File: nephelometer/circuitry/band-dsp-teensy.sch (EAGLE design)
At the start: 33 parts, among them IC1 LM4041CILP, IC2 AD822N, IC3 MCP6S21, J1 RJ11-6PTH, Q1 IRLB8721, T1 2N2222, T2 2N2222

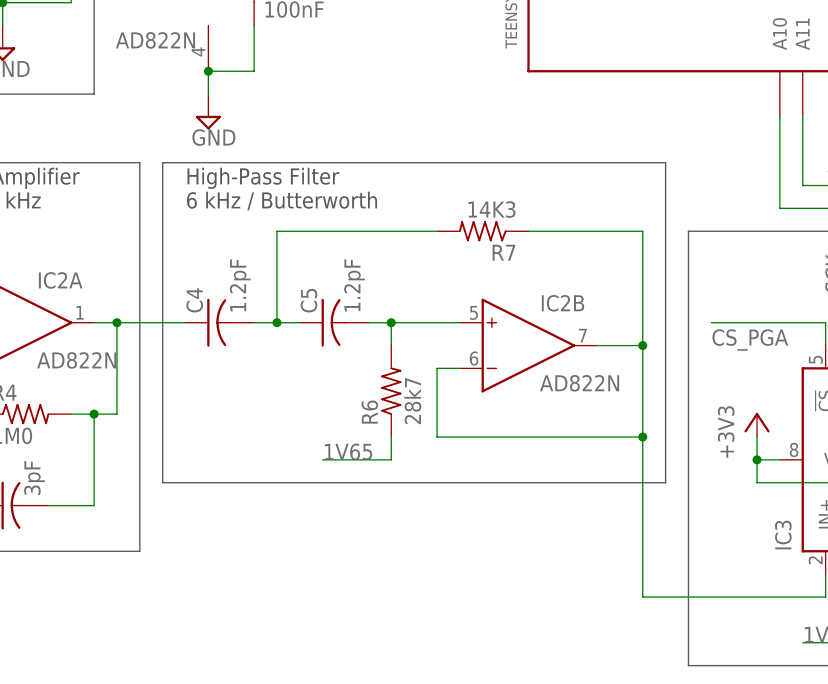
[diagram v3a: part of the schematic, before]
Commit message: Designed motor power board to stack on nephelometer or run over RJ11 cable
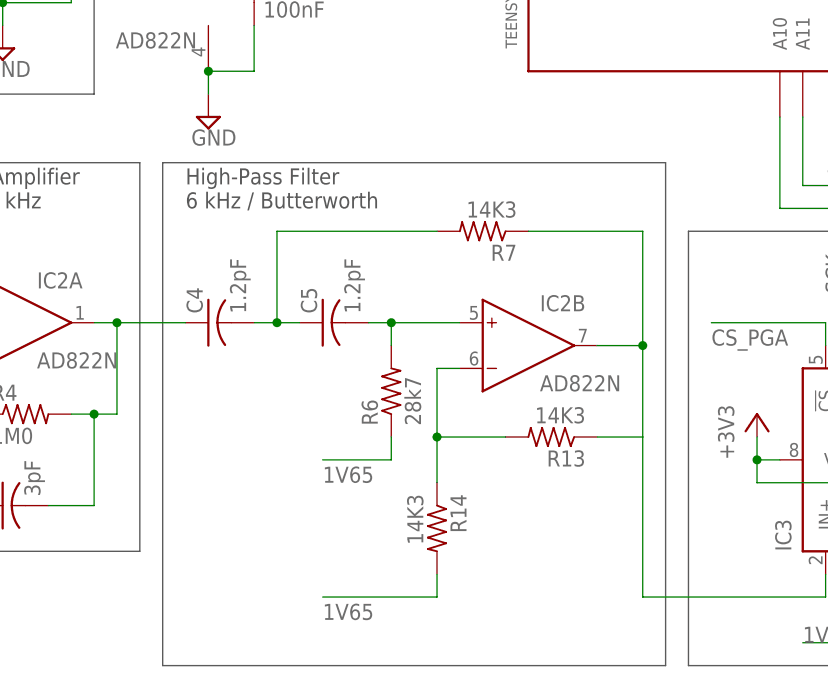
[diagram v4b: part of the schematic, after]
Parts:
- added R13, R14: 14K3, adafruit:R-US_0207/9
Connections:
- new net N$6: IC2B.IN-, R13.2, R14.1
- net 1V65: now also R14.2
- net N$3: now also R13.1; no longer IC2B.IN-
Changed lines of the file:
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@@
 <attribute name="MANF#" value="WP937AD/EGW"/>
+</part>
+<part name="R13" library="adafruit" deviceset="R-US_" device="0207/9" value="14K3">
+<attribute name="DIGIKEY#" value="14.3KXBK-ND"/>
+<attribute name="MANF" value="Yageo"/>
+<attribute name="MANF#" value="MFR-25FBF52-14K3"/>
+</part>
+<part name="R14" library="adafruit" deviceset="R-US_" device="0207/9" value="14K3">
+<attribute name="DIGIKEY#" value="14.3KXBK-ND"/>
+<attribute name="MANF" value="Yageo"/>
+<attribute name="MANF#" value="MFR-25FBF52-14K3"/>
 </part>
 </parts>
@@
 1 V / µA, fN = 194 kHz</text>
 <wire x1="109.22" y1="66.04" x2="109.22" y2="22.86" width="0.1524" layer="97"/>
-<wire x1="111.76" y1="66.04" x2="111.76" y2="30.48" width="0.1524" layer="97"/>
+<wire x1="111.76" y1="66.04" x2="111.76" y2="10.16" width="0.1524" layer="97"/>
 <wire x1="167.64" y1="66.04" x2="111.76" y2="66.04" width="0.1524" layer="97"/>
-<wire x1="111.76" y1="30.48" x2="167.64" y2="30.48" width="0.1524" layer="97"/>
-<wire x1="167.64" y1="66.04" x2="167.64" y2="30.48" width="0.1524" layer="97"/>
+<wire x1="111.76" y1="10.16" x2="167.64" y2="10.16" width="0.1524" layer="97"/>
+<wire x1="167.64" y1="66.04" x2="167.64" y2="10.16" width="0.1524" layer="97"/>
 <text x="114.3" y="60.96" size="1.778" layer="97">High-Pass Filter
 6 kHz / Butterworth</text>
@@
 <attribute name="MANF#" x="200.66" y="180.34" size="1.778" layer="96" rot="R180" display="off"/>
 </instance>
+<instance part="R13" gate="G$1" x="154.94" y="35.56" rot="R180">
+<attribute name="DIGIKEY#" x="154.94" y="35.56" size="1.778" layer="96" rot="R180" display="off"/>
+<attribute name="MANF" x="154.94" y="35.56" size="1.778" layer="96" rot="R180" display="off"/>
+<attribute name="MANF#" x="154.94" y="35.56" size="1.778" layer="96" rot="R180" display="off"/>
+</instance>
+<instance part="R14" gate="G$1" x="142.24" y="25.4" rot="R270">
+<attribute name="DIGIKEY#" x="142.24" y="25.4" size="1.778" layer="96" rot="R270" display="off"/>
+<attribute name="MANF" x="142.24" y="25.4" size="1.778" layer="96" rot="R270" display="off"/>
+<attribute name="MANF#" x="142.24" y="25.4" size="1.778" layer="96" rot="R270" display="off"/>
+</instance>
 </instances>
 <busses>
@@
 <wire x1="129.54" y1="33.02" x2="137.16" y2="33.02" width="0.1524" layer="91"/>
 <wire x1="137.16" y1="33.02" x2="137.16" y2="35.56" width="0.1524" layer="91"/>
-<label x="129.54" y="33.02" size="1.778" layer="95"/>
+<label x="129.54" y="30.48" size="1.778" layer="95"/>
 </segment>
 <segment>
@@
 <label x="182.88" y="12.7" size="1.778" layer="95"/>
 <pinref part="IC3" gate="G$1" pin="VREF"/>
+</segment>
+<segment>
+<pinref part="R14" gate="G$1" pin="2"/>
+<wire x1="142.24" y1="20.32" x2="142.24" y2="17.78" width="0.1524" layer="91"/>
+<wire x1="142.24" y1="17.78" x2="129.54" y2="17.78" width="0.1524" layer="91"/>
+<label x="129.54" y="15.24" size="1.778" layer="95"/>
 </segment>
 </net>
@@
 <pinref part="IC2" gate="B" pin="OUT"/>
 <wire x1="160.02" y1="45.72" x2="165.1" y2="45.72" width="0.1524" layer="91"/>
-<wire x1="165.1" y1="45.72" x2="165.1" y2="35.56" width="0.1524" layer="91"/>
-<wire x1="165.1" y1="35.56" x2="142.24" y2="35.56" width="0.1524" layer="91"/>
-<wire x1="142.24" y1="35.56" x2="142.24" y2="43.18" width="0.1524" layer="91"/>
-<pinref part="IC2" gate="B" pin="IN-"/>
-<wire x1="142.24" y1="43.18" x2="144.78" y2="43.18" width="0.1524" layer="91"/>
 <wire x1="165.1" y1="45.72" x2="165.1" y2="58.42" width="0.1524" layer="91"/>
 <junction x="165.1" y="45.72"/>
@@
 <wire x1="165.1" y1="58.42" x2="152.4" y2="58.42" width="0.1524" layer="91"/>
 <wire x1="165.1" y1="17.78" x2="165.1" y2="35.56" width="0.1524" layer="91"/>
-<junction x="165.1" y="35.56"/>
+<pinref part="R13" gate="G$1" pin="1"/>
+<wire x1="165.1" y1="35.56" x2="165.1" y2="45.72" width="0.1524" layer="91"/>
+<wire x1="165.1" y1="35.56" x2="160.02" y2="35.56" width="0.1524" layer="91"/>
 </segment>
 </net>
@@
 </segment>
 </net>
+<net name="N$6" class="0">
+<segment>
+<pinref part="IC2" gate="B" pin="IN-"/>
+<wire x1="142.24" y1="43.18" x2="144.78" y2="43.18" width="0.1524" layer="91"/>
+<wire x1="142.24" y1="35.56" x2="142.24" y2="43.18" width="0.1524" layer="91"/>
+<pinref part="R13" gate="G$1" pin="2"/>
+<wire x1="142.24" y1="35.56" x2="149.86" y2="35.56" width="0.1524" layer="91"/>
+<pinref part="R14" gate="G$1" pin="1"/>
+<wire x1="142.24" y1="30.48" x2="142.24" y2="35.56" width="0.1524" layer="91"/>
+<junction x="142.24" y="35.56"/>
+</segment>
+</net>

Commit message: Motor control with transistor gating MOSFET, shutoff when disconnected
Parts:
- C5: value 1.2pF -> 100nF; DIGIKEY# BC1026CT-ND -> BC1084CT-ND; MANF# K122J15C0GF5TL2 -> K104K15X7RF5TL2
- C6: value 100nF -> 1.2pF; DIGIKEY# BC1084CT-ND -> BC1026CT-ND; MANF# K104K15X7RF5TL2 -> K122J15C0GF5TL2
- R10: value 330R -> 14K3; DIGIKEY# CF14JT330RCT-ND -> 14.3KXBK-ND; MANF Stackpole Electronics Inc. -> Yageo; MANF# CF14JT330R -> MFR-25FBF52-14K3
- R11: value 330R -> 4K7; DIGIKEY# CF14JT330RCT-ND -> CF14JT4K70CT-ND; MANF Stackpole Electronics Inc. -> Stackpole Electronics Inc; MANF# CF14JT330R -> CF14JT4K70
- R12: value 150R -> 330R; DIGIKEY# CF14JT150RCT-ND -> CF14JT330RCT-ND; MANF# CF14JT150R -> CF14JT330R
- R13: value 14K3 -> 330R; DIGIKEY# 14.3KXBK-ND -> CF14JT330RCT-ND; MANF Yageo -> Stackpole Electronics Inc.; MANF# MFR-25FBF52-14K3 -> CF14JT330R
- R14: value 14K3 -> 150R; DIGIKEY# 14.3KXBK-ND -> CF14JT150RCT-ND; MANF Yageo -> Stackpole Electronics Inc.; MANF# MFR-25FBF52-14K3 -> CF14JT150R
- R8: value 4K7 -> 14K3; DIGIKEY# CF14JT4K70CT-ND -> 14.3KXBK-ND; MANF Stackpole Electronics Inc -> Yageo; MANF# CF14JT4K70 -> MFR-25FBF52-14K3
- renumbered JP1 to LED1, U$5 to LED3, U$6 to LED2
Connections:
- net +3V3: now also C5.1, R14.1; no longer C6.1, R12.1
- net +5V: now also R9.2; no longer R8.2
- net 1V65: now also R7.2; no longer R14.2
- net GND: now also C5.2, R12.1, R13.1; no longer C6.2, R10.1, R11.1
- net LEDCTRL: now also R11.2; no longer R9.2
- net N$10: now also D1.A; no longer D2.A
- net N$11: now also R14.2; no longer R12.2
- net N$12: now also R12.2; no longer R11.2
- net N$2: now also C6.1, R8.2; no longer C5.1, R7.2
- net N$3: now also R10.1, R8.1; no longer R13.1, R7.1
- net N$5: now also R11.1; no longer R9.1
- net N$6: now also R10.2, R7.1; no longer R13.2, R14.1
- net N$7: now also R13.2; no longer R10.2
- net N$8: now also R9.1; no longer R8.1
- net N$9: now also C6.2; no longer C5.2
- net V+: now also D2.A; no longer D1.A
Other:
- moved on the sheet: C5, C6, D1, D2, R10, R11, R12, R13, R14, R7, R8, R9

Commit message: Corrected resistor divider
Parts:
- R2: value 1K00 -> 3K01
- R3: value 3K01 -> 1K00
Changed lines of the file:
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@@
 <?xml version="1.0" encoding="utf-8"?>
 <!DOCTYPE eagle SYSTEM "eagle.dtd">
-<eagle version="7.5.0">
+<eagle version="7.7.0">
 <drawing>
 <settings>
@@
 <parts>
 <part name="SUPPLY2" library="supply2" deviceset="GND" device=""/>
-<part name="R2" library="adafruit" deviceset="R-US_" device="0207/9" value="1K00">
+<part name="R2" library="adafruit" deviceset="R-US_" device="0207/9" value="3K01">
 <attribute name="DIGIKEY#" value="RNF14FTD1K00CT-ND"/>
 <attribute name="MANF" value="Stackpole Electronics Inc."/>
@@
 <attribute name="MANF#" value="FK18C0G1H030C"/>
 </part>
-<part name="R3" library="adafruit" deviceset="R-US_" device="0207/9" value="3K01">
+<part name="R3" library="adafruit" deviceset="R-US_" device="0207/9" value="1K00">
 <attribute name="DIGIKEY#" value="RNF14FTD3K01CT-ND"/>
 <attribute name="MANF" value="Stackpole Electronics Inc."/>

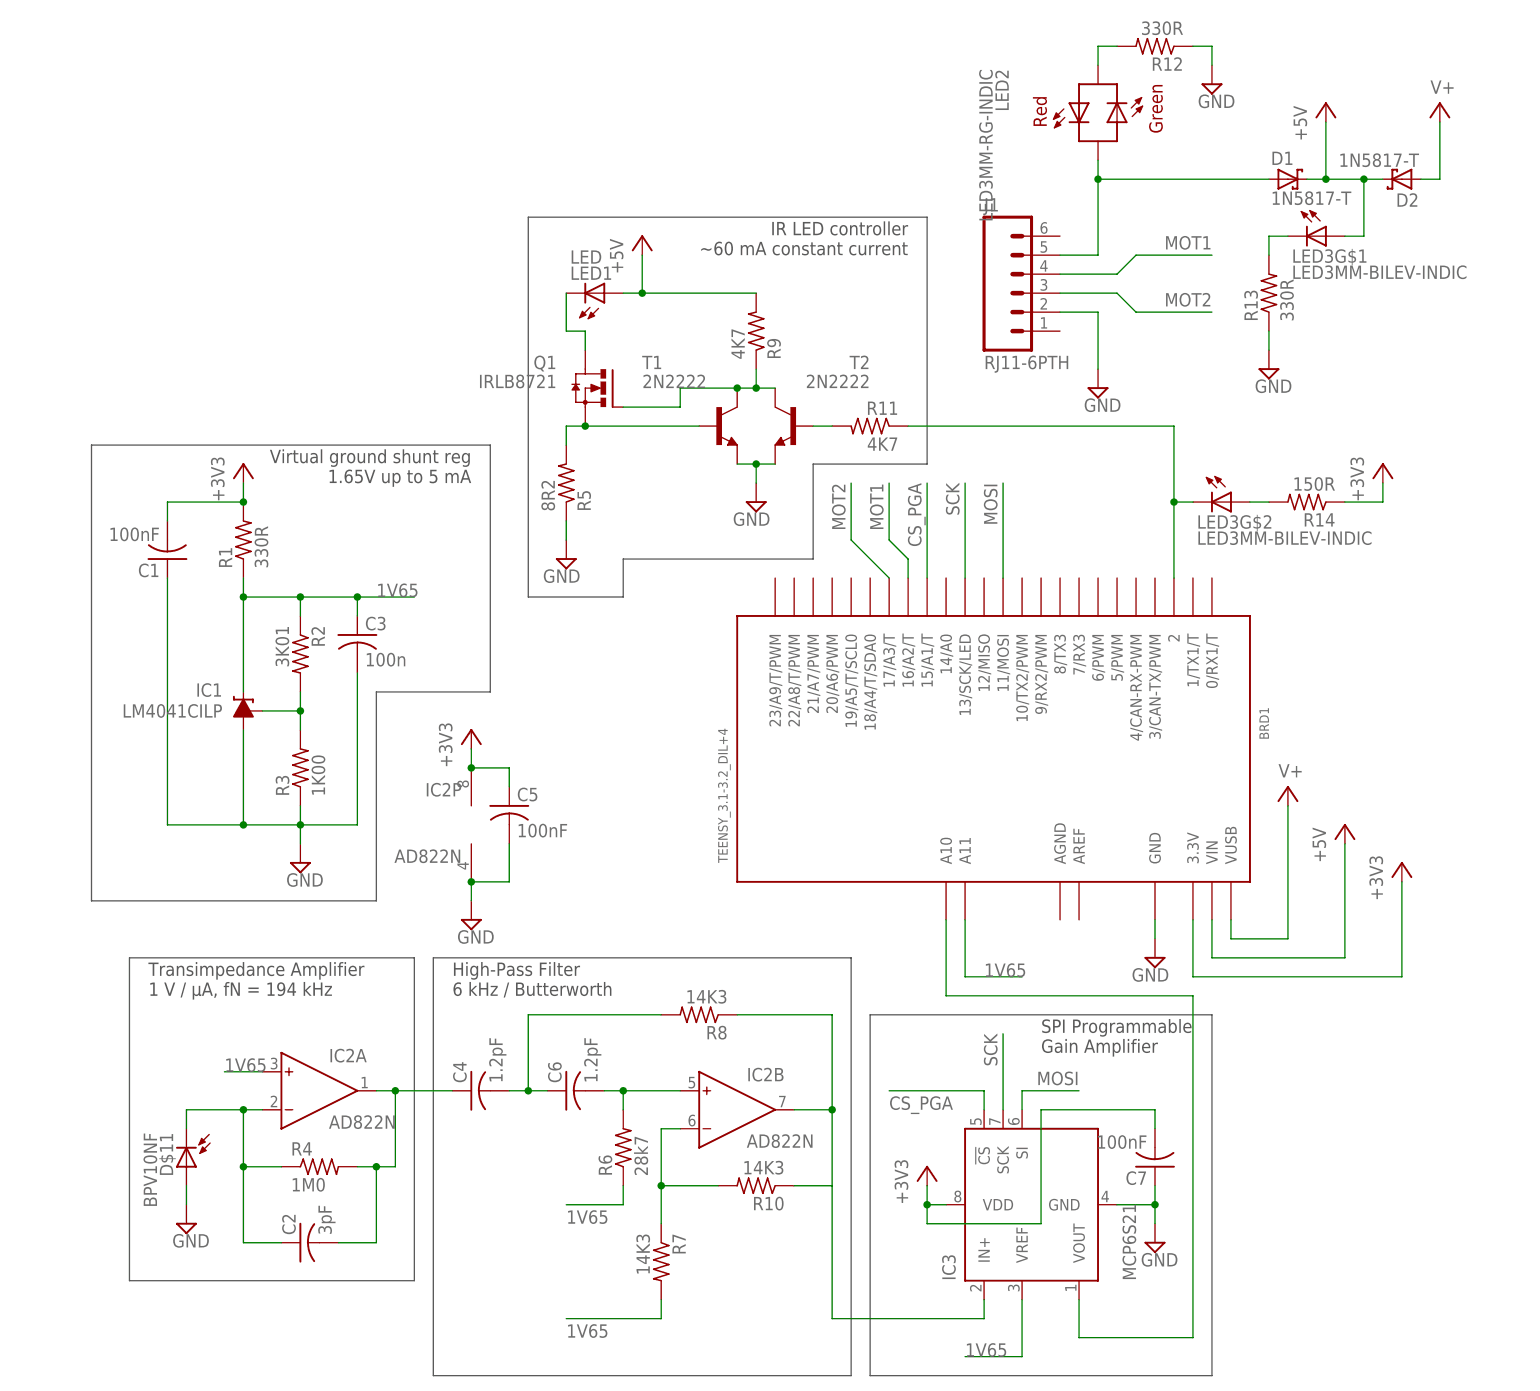
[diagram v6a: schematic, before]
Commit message: Revised detector board circuit, picked filter values, finalized parts
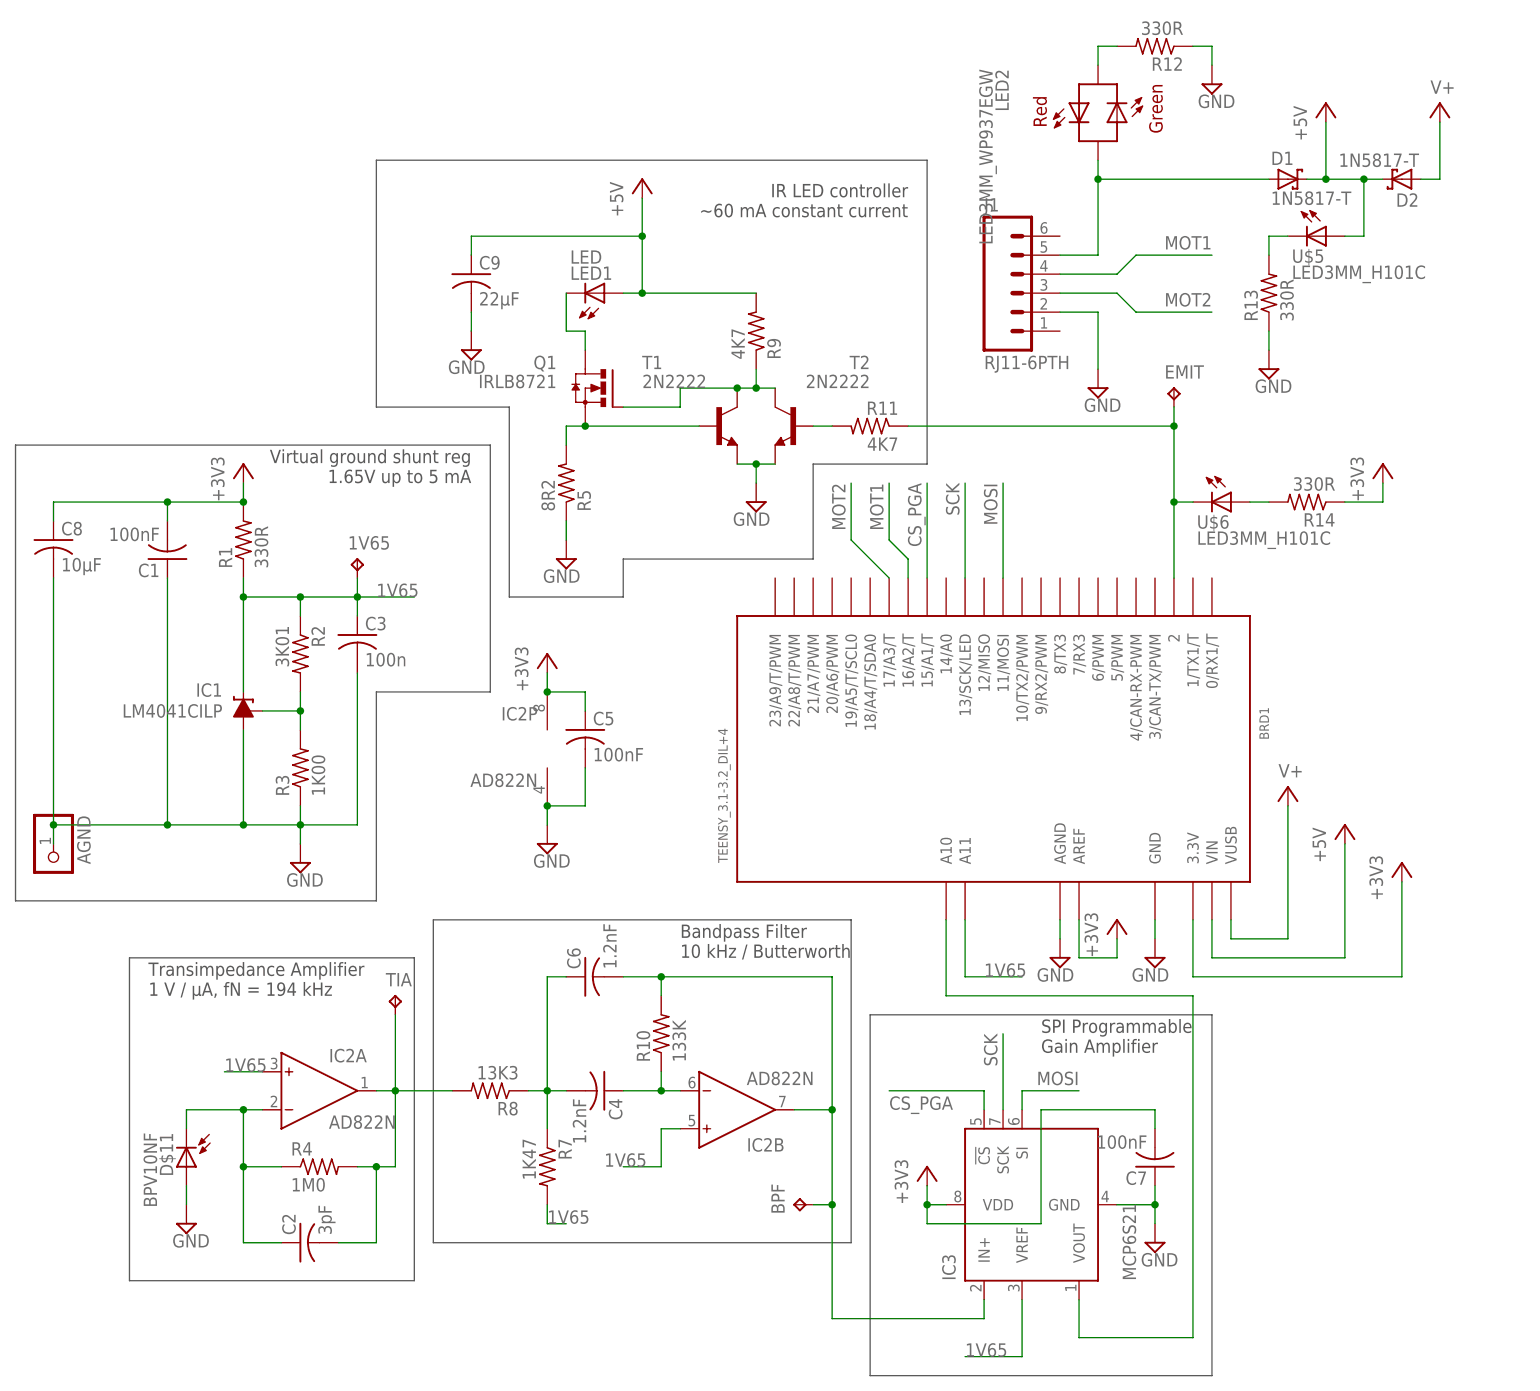
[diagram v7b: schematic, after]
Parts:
- removed LED3: LED3MM-BILEV-INDIC, ingolia:LED3MM-BILEV-INDIC
- removed R6: 28k7, adafruit:R-US_0207/9
- added 1V65, BPF, TIA: TPTP10R, testpad:TPTP10R
- added AGND: (no value), adafruit:PINHD-1X1
- added C8: 10µF, adafruit:C-US025-030X050
- added C9: 22µF, adafruit:C-US050-045X075
- added EMIT: TPPAD1-13, testpad:TPPAD1-13
- added U$5, U$6: LED3MM_H101C, ingolia:LED3MM_H101C
- BRD1: DIGIKEY2# 1568-1422-ND -> 300-1002-ND; DIGIKEY3# (none) -> SAM1198-14-ND; DIGIKEY4# (none) -> SAM1198-14-ND; DIGIKEY5# (none) -> S7038-ND; DIGIKEY6# (none) -> S7047-ND; DIGIKEY7# (none) -> S7047-ND; MANF2 SparkFun Electronics -> Citizen Finedevice Co Ltd; MANF2# PRT-13925 -> CFS-20632768DZFB; MANF3 (none) -> Samtec Inc.; MANF3# (none) -> SSQ-114-03-G-S; MANF4 (none) -> Samtec Inc.; MANF4# (none) -> SSQ-114-03-G-S; MANF5 (none) -> Sullins Connector Solutions; MANF5# (none) -> PPPC051LFBN-RC; MANF6 (none) -> Sullins Connector Solutions; MANF6# (none) -> PPPC141LFBN-RC; MANF7 (none) -> Sullins Connector Solutions; MANF7# (none) -> PPPC141LFBN-RC
- C4, C6: value 1.2pF -> 1.2nF
- LED1: DIGIKEY3# (none) -> ED2740-ND; MANF3 (none) -> On Shore Technology Inc.; MANF3# (none) -> OSTTE020104
- LED2: value LED3MM-RG-INDIC -> LED3MM_WP937EGW; device ingolia:LED3MM-RG-INDIC -> ingolia:LED3MM_WP937EGW; DIGIKEY# 754-1991-ND -> 754-1751-ND; DIGIKEY2# (none) -> 492-1789-ND; MANF# WP937AD/EGW -> WP937EGW; MANF2 (none) -> Bivar Inc.; MANF2# (none) -> H-101C
- Q1: device ingolia:IRLB8721 -> ingolia:IRLB8721HORIZONTAL
- R10: value 14K3 -> 133K; DIGIKEY# 14.3KXBK-ND -> 133KXBK-ND; MANF# MFR-25FBF52-14K3 -> MFR-25FBF52-133K
- R14: value 150R -> 330R
- R2: DIGIKEY# RNF14FTD1K00CT-ND -> RNF14FTD3K01CT-ND; MANF# RNF14FTD1K00 -> RNF14FTD3K01
- R3: DIGIKEY# RNF14FTD3K01CT-ND -> RNF14FTD1K00CT-ND; MANF# RNF14FTD3K01 -> RNF14FTD1K00
- R7: value 14K3 -> 1K47; DIGIKEY# 14.3KXBK-ND -> 1.50KXBK-ND; MANF# MFR-25FBF52-14K3 -> MFR-25FBF52-1K5
- R8: value 14K3 -> 13K3; DIGIKEY# 14.3KXBK-ND -> 13.3KXBK-ND; MANF# MFR-25FBF52-14K3 -> MFR-25FBF52-13K3
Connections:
- removed net N$2: C4.2, C6.1, R8.2
- net +3V3: now also BRD1.AREF, C8.1
- net +5V: now also C9.1, U$5.A; no longer LED3G$1.A
- net 1V65: now also 1V65.TP, IC2B.IN+; no longer R6.1
- net GND: now also AGND.1, BRD1.AGND, C8.2, C9.2
- net N$11: now also U$6.A; no longer LED3G$2.A
- net N$22: now also R8.2, TIA.TP; no longer C4.1
- net N$3: now also C4.2, C6.1, R7.1; no longer IC2B.OUT, IC3.IN+, R10.1
- net N$5: now also EMIT.TP, U$6.K; no longer LED3G$2.K
- net N$6: now also BPF.TP, C6.2, IC2B.OUT, IC3.IN+; no longer IC2B.IN-, R7.1
- net N$7: now also U$5.K; no longer LED3G$1.K
- net N$9: now also C4.1, IC2B.IN-, R10.1; no longer C6.2, IC2B.IN+, R6.2
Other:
- note added: "Bandpass Filter 10 kHz / Butterworth"
- note removed: "High-Pass Filter 6 kHz / Butterworth"
- moved on the sheet: C4, C5, C6, IC2B, IC2P, R10, R7, R8
